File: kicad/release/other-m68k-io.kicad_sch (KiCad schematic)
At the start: 37 parts, among them J11 FTDI B (GND CTS VCC TXD RXD R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, J12 Joystick (Atari DE-9), J2 FTDI (GND CTS VCC TXD RXD RTS), Q1 MMDT3904, SW1 RESET, U10 MC68681P, U13 MCP130T-450I/TT, U14 74HC14, Y1 3.6864MHz

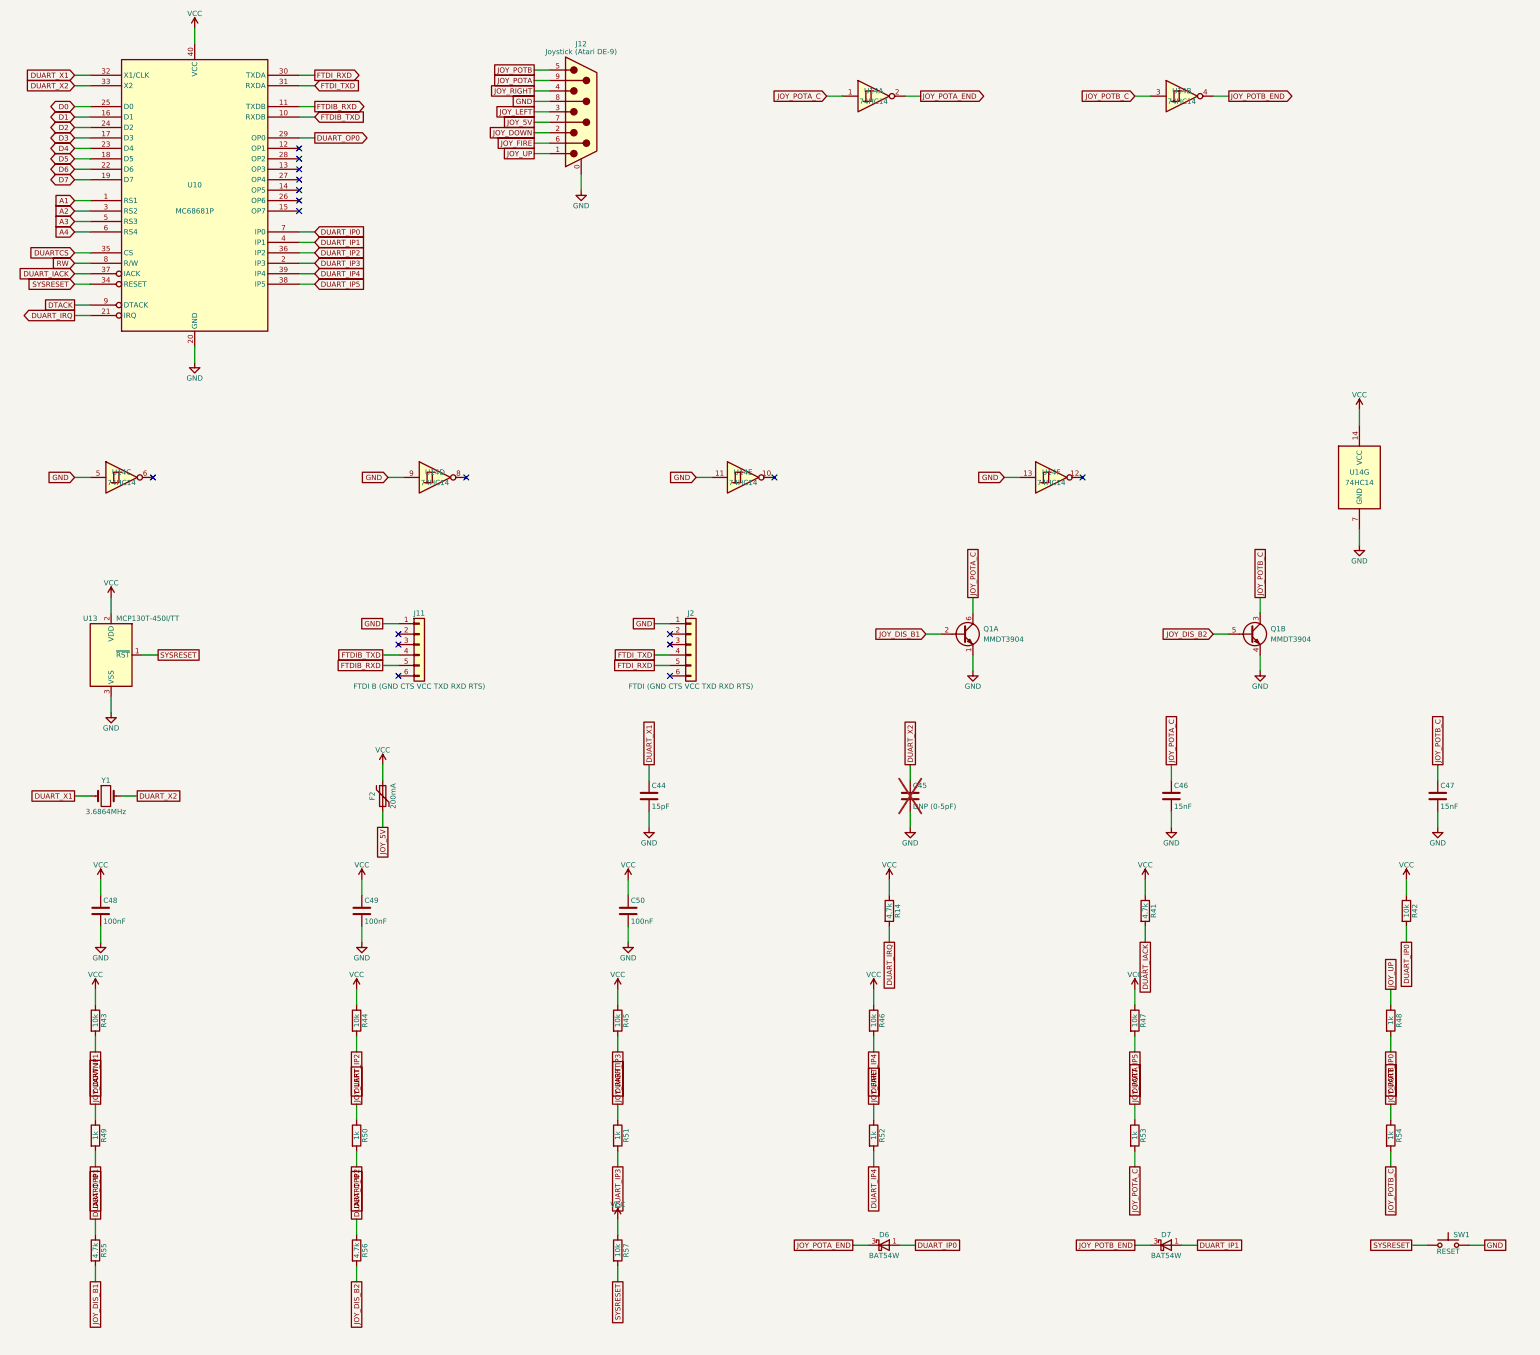
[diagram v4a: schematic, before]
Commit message: spec rev 12 / board rev C3: serial header B powers its device; OP1 on its RTS pin
J11 pin 3 carries 5 V through F3 (200 mA polyfuse) and D8 (BAT54W, so a 5 V FTDI cable
plugged in there cannot back-feed the board) for the serial-mouse MAX232 adapter; pin 6
(RTS) is DUART OP1 so firmware can switch the mouse's RTS/DTR power and provoke its
identification byte. J2 keeps GND, TXD, RXD only. Routed with the optimizer off after
moving the analyser's resistor arrays 1.5 mm from the header: 0 DRC violations, 0
unrouted; fab package and release regenerated. Spec, KiCad README, ORDER.md, architecture
and the programmer's guide (2.11 channel B) describe it; no firmware change.

Co-Authored-By: Claude Fable 5.1 <noreply@anthropic.com>
Claude-Session: https://claude.ai/code/session_019bbFLKMxhKXGW6aABP44Z1
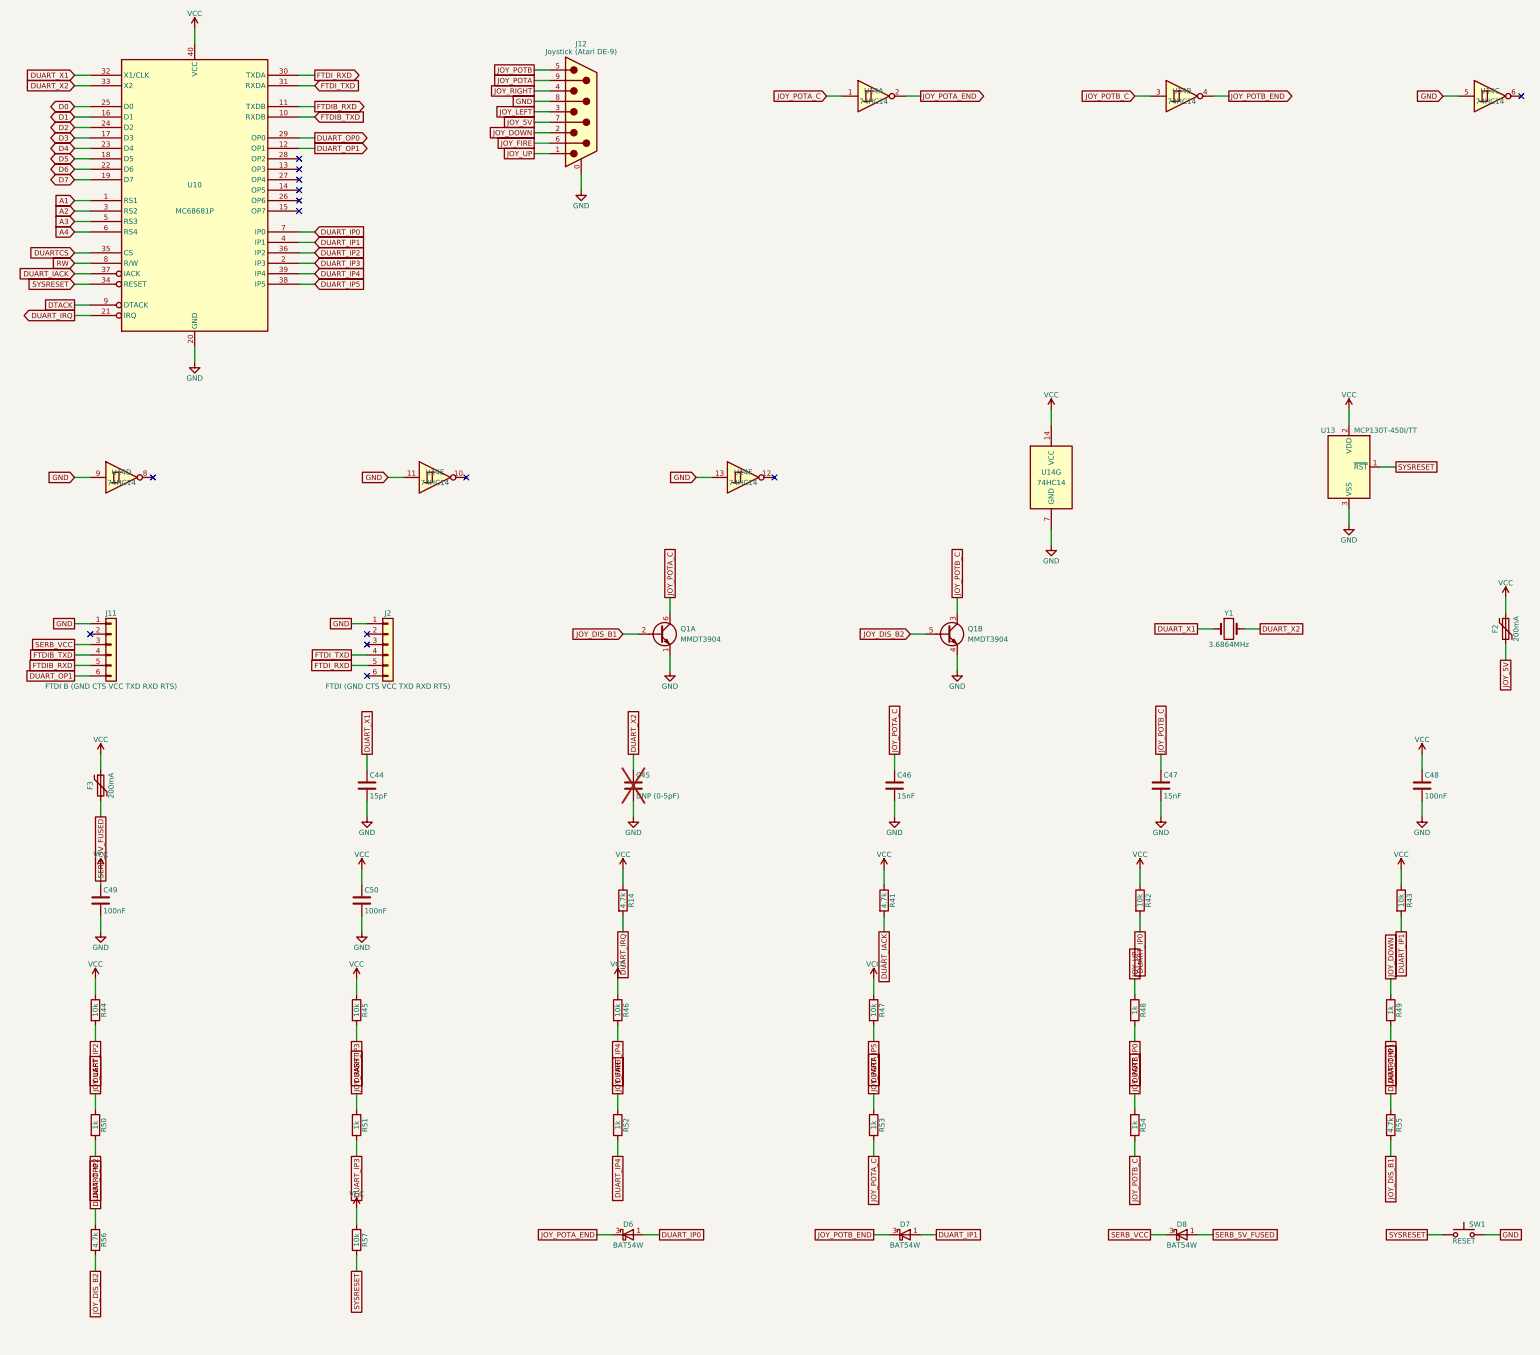
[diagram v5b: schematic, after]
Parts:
- added D8: BAT54W, Package_TO_SOT_SMD:SOT-323_SC-70, symbol Diode:BAT54W
- added F3: 200mA, Fuse:Fuse_1206_3216Metric, symbol Device:Polyfuse
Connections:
- net VCC: now also F3.1
- net SERB_VCC: now reaches J11.3 (Pin_3)
- net SERB_VCC: now also D8.3 (K)
- net DUART_OP1: now reaches J11.6 (Pin_6)
- net DUART_OP1: now also U10.12 (OP1)
- new net SERB_5V_FUSED: D8.1 (A), F3.2
- no-connect marks 17 -> 14
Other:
- moved on the sheet: C44, C45, C46, C47, C48, C49, C50, D6, D7, F2, J11, J2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

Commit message: rev C3 BOM: in-stock substitutes from the PCBWay quote: ECS-2200B-240 oscillator, Assmann PLCC-84 and DIP-40 sockets, generic DIP-64 socket acceptable
Co-Authored-By: Claude Fable 5.1 <noreply@anthropic.com>
Claude-Session: https://claude.ai/code/session_019bbFLKMxhKXGW6aABP44Z1
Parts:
- U10: Socket_Desc DIP-40 socket, 15.24 mm rows, gold contacts, RoHS -> DIP-40 socket, 15.24 mm rows, stamped dual-wipe tin contact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; Socket_MPN 110-43-640-41-001000 -> A 40-LC-TT; Socket_Manufacturer Mill-Max -> Assmann WSW
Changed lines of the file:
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@@
 			)
 		)
-		(property "Socket_Manufacturer" "Mill-Max"
+		(property "Socket_Manufacturer" "Assmann WSW"
 			(at 69.85 63.5 0)
 			(effects
@@
 			)
 		)
-		(property "Socket_MPN" "110-43-640-41-001000"
+		(property "Socket_MPN" "A 40-LC-TT"
 			(at 69.85 63.5 0)
 			(effects
@@
 			)
 		)
-		(property "Socket_Desc" "DIP-40 socket, 15.24 mm rows, gold contacts, RoHS"
+		(property "Socket_Desc" "DIP-40 socket, 15.24 mm rows, stamped dual-wipe tin contacts (same family as the DIP-32 sockets; A 40-LC-TR at DigiKey)"
 			(at 69.85 63.5 0)
 			(effects

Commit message: BOM: PCBWay descriptions carry only the part and its substitution rule; our sourcing remarks move to a Note field in parts.json, the KiCad BOM and the customer-parts list
Co-Authored-By: Claude Fable 5.1 <noreply@anthropic.com>
Claude-Session: https://claude.ai/code/session_019bbFLKMxhKXGW6aABP44Z1
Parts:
- C46, C47: Desc 15 nF 50 V X7R 0603 (Avnet/Future stock; any 0603 X7R 15 nF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 -> 15 nF 50 V X7R 0603; any 0603 X7R 15 nF 50 V is acceptable; Note (none) -> Avnet/Future stock the Samsung part
- D6, D7, D8: Desc Schottky diode 30 V 200 mA, SOT-323 (DigiKey/Mouser/LCSC st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 -> Schottky diode 30 V 200 mA, SOT-323; Note (none) -> DigiKey/Mouser/LCSC stocked
- F2, F3: Desc PTC resettable fuse 0.2 A hold / 0.42 A trip, 24 V, 1206 (D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 -> PTC resettable fuse 0.2 A hold / 0.42 A trip, 24 V, 1206; Note (none) -> DigiKey/Element14
- J12: Desc DE-9 male (plug), right angle, housed, 4-40 boardlocks, .318 in (8.08 mm) backset = KiCad's EdgePinOffset7.70/MountingHolesOffset9.12 footprint; DigiKey stocks it as L717SDE09PA4CH4FA610, Farnell as L717SDE09PA4CH4F (any L717SDE09PA4CH4x is the same connector) -> DE-9 male (plug), right angle, housed, 4-40 boardlocks, .318 in (8.08 mm) backset; any L717SDE09PA4CH4x is the same connector; Note (none) -> The .318 in backset is KiCad's EdgePinOffset7.70/MountingHo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
- U10: Socket_Desc DIP-40 socket, 15.24 mm rows, stamped dual-wipe tin contact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 -> DIP-40 socket, 15.24 mm rows, stamped dual-wipe tin contacts; Socket_Note (none) -> Same family as the DIP-32 sockets; A 40-LC-TR at DigiKey. R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
- Y1: Desc 3.6864 MHz crystal HC-49/US, 20 pF (-40..85 C grade; ECS-36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 -> 3.6864 MHz crystal HC-49/US, 20 pF; Note (none) -> -40..85 C grade; the commercial ECS-36-20-4DN is NRND
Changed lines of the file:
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@@
 			)
 		)
-		(property "Desc" "Schottky diode 30 V 200 mA, SOT-323 (DigiKey/Mouser/LCSC stocked)"
+		(property "Desc" "Schottky diode 30 V 200 mA, SOT-323"
+			(at 242.57 314.96 0)
+			(effects
+				(font
+					(size 1.27 1.27)
+				)
+				(hide yes)
+			)
+		)
+		(property "Note" "DigiKey/Mouser/LCSC stocked"
 			(at 242.57 314.96 0)
 			(effects
@@
 			)
 		)
-		(property "Desc" "15 nF 50 V X7R 0603 (Avnet/Future stock; any 0603 X7R 15 nF 50 V is fine)"
+		(property "Desc" "15 nF 50 V X7R 0603; any 0603 X7R 15 nF 50 V is acceptable"
+			(at 304.8 205.74 0)
+			(effects
+				(font
+					(size 1.27 1.27)
+				)
+				(hide yes)
+			)
+		)
+		(property "Note" "Avnet/Future stock the Samsung part"
 			(at 304.8 205.74 0)
 			(effects
@@
 			)
 		)
-		(property "Desc" "Schottky diode 30 V 200 mA, SOT-323 (DigiKey/Mouser/LCSC stocked)"
+		(property "Desc" "Schottky diode 30 V 200 mA, SOT-323"
+			(at 175.26 314.96 0)
+			(effects
+				(font
+					(size 1.27 1.27)
+				)
+				(hide yes)
+			)
+		)
+		(property "Note" "DigiKey/Mouser/LCSC stocked"
 			(at 175.26 314.96 0)
 			(effects
@@
 			)
 		)
-		(property "Desc" "15 nF 50 V X7R 0603 (Avnet/Future stock; any 0603 X7R 15 nF 50 V is fine)"
+		(property "Desc" "15 nF 50 V X7R 0603; any 0603 X7R 15 nF 50 V is acceptable"
+			(at 240.03 205.74 0)
+			(effects
+				(font
+					(size 1.27 1.27)
+				)
+				(hide yes)
+			)
+		)
+		(property "Note" "Avnet/Future stock the Samsung part"
 			(at 240.03 205.74 0)
 			(effects
@@
 			)
 		)
-		(property "Desc" "Schottky diode 30 V 200 mA, SOT-323 (DigiKey/Mouser/LCSC stocked)"
+		(property "Desc" "Schottky diode 30 V 200 mA, SOT-323"
+			(at 309.88 314.96 0)
+			(effects
+				(font
+					(size 1.27 1.27)
+				)
+				(hide yes)
+			)
+		)
+		(property "Note" "DigiKey/Mouser/LCSC stocked"
 			(at 309.88 314.96 0)
 			(effects
@@
 			)
 		)
-		(property "Desc" "PTC resettable fuse 0.2 A hold / 0.42 A trip, 24 V, 1206 (DigiKey/Element14)"
+		(property "Desc" "PTC resettable fuse 0.2 A hold / 0.42 A trip, 24 V, 1206"
+			(at 46.99 205.74 0)
+			(effects
+				(font
+					(size 1.27 1.27)
+				)
+				(hide yes)
+			)
+		)
+		(property "Note" "DigiKey/Element14"
 			(at 46.99 205.74 0)
 			(effects
@@
 			)
 		)
-		(property "Desc" "PTC resettable fuse 0.2 A hold / 0.42 A trip, 24 V, 1206 (DigiKey/Element14)"
+		(property "Desc" "PTC resettable fuse 0.2 A hold / 0.42 A trip, 24 V, 1206"
+			(at 388.62 167.64 0)
+			(effects
+				(font
+					(size 1.27 1.27)
+				)
+				(hide yes)
+			)
+		)
+		(property "Note" "DigiKey/Element14"
 			(at 388.62 167.64 0)
 			(effects
@@
 			)
 		)
-		(property "Desc" "DE-9 male (plug), right angle, housed, 4-40 boardlocks, .318 in (8.08 mm) backset = KiCad's EdgePinOffset7.70/MountingHolesOffset9.12 footprint; DigiKey stocks it as L717SDE09PA4CH4FA610, Farnell as L717SDE09PA4CH4F (any L717SDE09PA4CH4x is the same connector)"
+		(property "Desc" "DE-9 male (plug), right angle, housed, 4-40 boardlocks, .318 in (8.08 mm) backset; any L717SDE09PA4CH4x is the same connector"
+			(at 163.83 41.91 0)
+			(effects
+				(font
+					(size 1.27 1.27)
+				)
+				(hide yes)
+			)
+		)
+		(property "Note" "The .318 in backset is KiCad's EdgePinOffset7.70/MountingHolesOffset9.12 footprint. DigiKey stocks it as L717SDE09PA4CH4FA610, Farnell as L717SDE09PA4CH4F"
 			(at 163.83 41.91 0)
 			(effects
@@
 			)
 		)
-		(property "Desc" "3.6864 MHz crystal HC-49/US, 20 pF (-40..85 C grade; ECS-36-20-4DN is NRND)"
+		(property "Desc" "3.6864 MHz crystal HC-49/US, 20 pF"
+			(at 321.31 167.64 0)
+			(effects
+				(font
+					(size 1.27 1.27)
+				)
+				(hide yes)
+			)
+		)
+		(property "Note" "-40..85 C grade; the commercial ECS-36-20-4DN is NRND"
 			(at 321.31 167.64 0)
 			(effects
@@
 			)
 		)
-		(property "Socket_Desc" "DIP-40 socket, 15.24 mm rows, stamped dual-wipe tin contacts (same family as the DIP-32 sockets; A 40-LC-TR at DigiKey)"
+		(property "Socket_Desc" "DIP-40 socket, 15.24 mm rows, stamped dual-wipe tin contacts"
+			(at 69.85 63.5 0)
+			(effects
+				(font
+					(size 1.27 1.27)
+				)
+				(hide yes)
+			)
+		)
+		(property "Socket_Note" "Same family as the DIP-32 sockets; A 40-LC-TR at DigiKey. Replaces the Mill-Max PCBWay quoted at $22"
 			(at 69.85 63.5 0)
 			(effects
